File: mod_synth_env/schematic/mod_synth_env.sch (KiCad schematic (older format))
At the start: 26 parts, among them J1 AudioJack2, J2 AudioJack2, J3 Conn_02x08_Odd_Even, SW1 SW_Push, SW2 SW_SPDT, U1 TL072

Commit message: Add some footprints
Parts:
- D4: footprint (none) -> LED_THT:LED_D5.0mm
- J1, J2: footprint (none) -> Connector_Audio:Jack_3.5mm_QingPu_WQP-PJ398SM_Vertical_CircularHoles
- J3: footprint (none) -> Connector_IDC:IDC-Header_2x08_P2.54mm_Vertical
- RV1, RV2: footprint (none) -> Potentiometer_THT:Potentiometer_Alpha_RD901F-40-00D_Single_Vertical_CircularHoles
- U1: footprint (none) -> Package_DIP:DIP-8_W7.62mm_Socket_LongPads
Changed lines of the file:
@@
 EESchema Schematic File Version 4
+LIBS:mod_synth_env-cache
 EELAYER 29 0
 EELAYER END
@@
 F 0 "J3" H 3450 5742 50  0000 C CNN
 F 1 "Conn_02x08_Odd_Even" H 3450 5651 50  0000 C CNN
-F 2 "" H 3400 5225 50  0001 C CNN
+F 2 "Connector_IDC:IDC-Header_2x08_P2.54mm_Vertical" H 3400 5225 50  0001 C CNN
 F 3 "~" H 3400 5225 50  0001 C CNN
 	1    3400 5225
@@
 F 0 "J1" H 1607 3190 50  0000 C CNN
 F 1 "AudioJack2" H 1607 3099 50  0000 C CNN
-F 2 "" H 1575 2775 50  0001 C CNN
+F 2 "Connector_Audio:Jack_3.5mm_QingPu_WQP-PJ398SM_Vertical_CircularHoles" H 1575 2775 50  0001 C CNN
 F 3 "~" H 1575 2775 50  0001 C CNN
 F 4 "Gate In" H 1607 3008 50  0000 C CNN "Text"
@@
 F 0 "J2" H 1832 6915 50  0000 C CNN
 F 1 "AudioJack2" H 1832 6824 50  0000 C CNN
-F 2 "" H 1800 6500 50  0001 C CNN
+F 2 "Connector_Audio:Jack_3.5mm_QingPu_WQP-PJ398SM_Vertical_CircularHoles" H 1800 6500 50  0001 C CNN
 F 3 "~" H 1800 6500 50  0001 C CNN
 F 4 "Envelope Out" H 1832 6733 50  0000 C CNN "Text"
@@
 F 0 "RV2" H 6856 2616 50  0000 R CNN
 F 1 "1M" H 6856 2525 50  0000 R CNN
-F 2 "" H 6925 2525 50  0001 C CNN
+F 2 "Potentiometer_THT:Potentiometer_Alpha_RD901F-40-00D_Single_Vertical_CircularHoles" H 6925 2525 50  0001 C CNN
 F 3 "~" H 6925 2525 50  0001 C CNN
 F 4 "Attack" H 6856 2434 50  0000 R CNN "Text"
@@
 F 0 "RV1" H 6830 3341 50  0000 R CNN
 F 1 "1M" H 6830 3250 50  0000 R CNN
-F 2 "" H 6900 3250 50  0001 C CNN
+F 2 "Potentiometer_THT:Potentiometer_Alpha_RD901F-40-00D_Single_Vertical_CircularHoles" H 6900 3250 50  0001 C CNN
 F 3 "~" H 6900 3250 50  0001 C CNN
 F 4 "Release" H 6830 3159 50  0000 R CNN "Text"
@@
 F 0 "D4" H 3568 6245 50  0000 C CNN
 F 1 "LED" H 3568 6336 50  0000 C CNN
-F 2 "" H 3575 6500 50  0001 C CNN
+F 2 "LED_THT:LED_D5.0mm" H 3575 6500 50  0001 C CNN
 F 3 "~" H 3575 6500 50  0001 C CNN
 	1    3575 6500
@@
 F 0 "U1" H 1700 4492 50  0000 C CNN
 F 1 "TL072" H 1700 4401 50  0000 C CNN
-F 2 "" H 1700 4125 50  0001 C CNN
+F 2 "Package_DIP:DIP-8_W7.62mm_Socket_LongPads" H 1700 4125 50  0001 C CNN
 F 3 "http://www.ti.com/lit/ds/symlink/tl071.pdf" H 1700 4125 50  0001 C CNN
 	1    1700 4125

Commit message: Add footprints
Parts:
- C1, C2: footprint (none) -> Capacitor_THT:C_Disc_D9.0mm_W2.5mm_P5.00mm
- R1, R2, R3, R4, R5, R6, R7, R8, R9: footprint (none) -> Resistor_THT:R_Axial_DIN0207_L6.3mm_D2.5mm_P10.16mm_Horizontal
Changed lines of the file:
@@
 F 0 "R7" V 3668 3425 50  0000 C CNN
 F 1 "100k" V 3759 3425 50  0000 C CNN
-F 2 "" V 3805 3425 50  0001 C CNN
+F 2 "Resistor_THT:R_Axial_DIN0207_L6.3mm_D2.5mm_P10.16mm_Horizontal" V 3805 3425 50  0001 C CNN
 F 3 "~" H 3875 3425 50  0001 C CNN
 	1    3875 3425
@@
 F 0 "R8" V 4293 3425 50  0000 C CNN
 F 1 "47k" V 4384 3425 50  0000 C CNN
-F 2 "" V 4430 3425 50  0001 C CNN
+F 2 "Resistor_THT:R_Axial_DIN0207_L6.3mm_D2.5mm_P10.16mm_Horizontal" V 4430 3425 50  0001 C CNN
 F 3 "~" H 4500 3425 50  0001 C CNN
 	1    4500 3425
@@
 F 0 "R9" H 5520 2896 50  0000 L CNN
 F 1 "100k" H 5520 2805 50  0000 L CNN
-F 2 "" V 5380 2850 50  0001 C CNN
+F 2 "Resistor_THT:R_Axial_DIN0207_L6.3mm_D2.5mm_P10.16mm_Horizontal" V 5380 2850 50  0001 C CNN
 F 3 "~" H 5450 2850 50  0001 C CNN
 	1    5450 2850
@@
 F 0 "R1" H 995 4221 50  0000 L CNN
 F 1 "100k" H 995 4130 50  0000 L CNN
-F 2 "" V 855 4175 50  0001 C CNN
+F 2 "Resistor_THT:R_Axial_DIN0207_L6.3mm_D2.5mm_P10.16mm_Horizontal" V 855 4175 50  0001 C CNN
 F 3 "~" H 925 4175 50  0001 C CNN
 	1    925  4175
@@
 F 0 "R2" H 1095 4571 50  0000 L CNN
 F 1 "10k" H 1095 4480 50  0000 L CNN
-F 2 "" V 955 4525 50  0001 C CNN
+F 2 "Resistor_THT:R_Axial_DIN0207_L6.3mm_D2.5mm_P10.16mm_Horizontal" V 955 4525 50  0001 C CNN
 F 3 "~" H 1025 4525 50  0001 C CNN
 	1    1025 4525
@@
 F 0 "R3" H 1295 5696 50  0000 L CNN
 F 1 "47k" H 1295 5605 50  0000 L CNN
-F 2 "" V 1155 5650 50  0001 C CNN
+F 2 "Resistor_THT:R_Axial_DIN0207_L6.3mm_D2.5mm_P10.16mm_Horizontal" V 1155 5650 50  0001 C CNN
 F 3 "~" H 1225 5650 50  0001 C CNN
 	1    1225 5650
@@
 F 0 "R4" H 2245 6146 50  0000 L CNN
 F 1 "1k" H 2245 6055 50  0000 L CNN
-F 2 "" V 2105 6100 50  0001 C CNN
+F 2 "Resistor_THT:R_Axial_DIN0207_L6.3mm_D2.5mm_P10.16mm_Horizontal" V 2105 6100 50  0001 C CNN
 F 3 "~" H 2175 6100 50  0001 C CNN
 	1    2175 6100
@@
 F 0 "R5" V 2093 3575 50  0000 C CNN
 F 1 "R100k" V 2184 3575 50  0000 C CNN
-F 2 "" V 2230 3575 50  0001 C CNN
+F 2 "Resistor_THT:R_Axial_DIN0207_L6.3mm_D2.5mm_P10.16mm_Horizontal" V 2230 3575 50  0001 C CNN
 F 3 "~" H 2300 3575 50  0001 C CNN
 	1    2300 3575
@@
 F 0 "R6" V 2943 6500 50  0000 C CNN
 F 1 "1k" V 3034 6500 50  0000 C CNN
-F 2 "" V 3080 6500 50  0001 C CNN
+F 2 "Resistor_THT:R_Axial_DIN0207_L6.3mm_D2.5mm_P10.16mm_Horizontal" V 3080 6500 50  0001 C CNN
 F 3 "~" H 3150 6500 50  0001 C CNN
 	1    3150 6500
@@
 F 0 "C2" H 4515 2896 50  0000 L CNN
 F 1 "10nF" H 4515 2805 50  0000 L CNN
-F 2 "" H 4438 2700 50  0001 C CNN
+F 2 "Capacitor_THT:C_Disc_D9.0mm_W2.5mm_P5.00mm" H 4438 2700 50  0001 C CNN
 F 3 "~" H 4400 2850 50  0001 C CNN
 	1    4400 2850
@@
 F 0 "C1" H 2440 4696 50  0000 L CNN
 F 1 "1uF" H 2440 4605 50  0000 L CNN
-F 2 "" H 2363 4500 50  0001 C CNN
+F 2 "Capacitor_THT:C_Disc_D9.0mm_W2.5mm_P5.00mm" H 2363 4500 50  0001 C CNN
 F 3 "~" H 2325 4650 50  0001 C CNN
 	1    2325 4650

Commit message: Start work on envelope PCB
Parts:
- SW1: footprint (none) -> Connector_PinHeader_1.00mm:PinHeader_1x02_P1.00mm_Vertical
- SW2: footprint (none) -> Connector_PinHeader_1.00mm:PinHeader_1x03_P1.00mm_Vertical
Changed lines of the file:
@@
 F 0 "SW2" H 2975 3410 50  0000 C CNN
 F 1 "SW_SPDT" H 2975 3319 50  0000 C CNN
-F 2 "" H 2975 3125 50  0001 C CNN
+F 2 "Connector_PinHeader_1.00mm:PinHeader_1x03_P1.00mm_Vertical" H 2975 3125 50  0001 C CNN
 F 3 "~" H 2975 3125 50  0001 C CNN
 	1    2975 3125
-	1    0    0    -1
-$EndComp
-$Comp
-L Switch:SW_Push SW1
-U 1 1 5D201272
-P 2375 2500
-F 0 "SW1" H 2375 2785 50  0000 C CNN
-F 1 "SW_Push" H 2375 2694 50  0000 C CNN
-F 2 "" H 2375 2700 50  0001 C CNN
-F 3 "~" H 2375 2700 50  0001 C CNN
-	1    2375 2500
 	1    0    0    -1
 $EndComp
@@
 	1950 3125 2175 3125
 Wire Wire Line
-	2475 3125 2575 3125
-Wire Wire Line
-	2575 2500 2575 3125
-Connection ~ 2575 3125
-Wire Wire Line
-	2575 3125 2775 3125
+	3900 4725 4200 4725
+Wire Wire Line
+	4200 4725 4200 4875
+Connection ~ 3900 4725
+Wire Wire Line
+	3900 4725 3900 4925
+Wire Wire Line
+	4200 5500 4200 5625
+Wire Wire Line
+	4200 5625 3900 5625
+Connection ~ 3900 5625
+Wire Wire Line
+	3900 5625 3900 5325
+Wire Wire Line
+	2000 6400 2000 5350
+Wire Wire Line
+	2000 5125 2325 5125
+Connection ~ 2650 5125
+Wire Wire Line
+	2000 6500 2175 6500
+Wire Wire Line
+	2175 6500 3000 6500
+Connection ~ 2175 6500
+Wire Wire Line
+	3300 6500 3425 6500
+$Comp
+L power:GND #PWR0105
+U 1 1 5D257A03
+P 4125 6500
+F 0 "#PWR0105" H 4125 6250 50  0001 C CNN
+F 1 "GND" H 4130 6327 50  0000 C CNN
+F 2 "" H 4125 6500 50  0001 C CNN
+F 3 "" H 4125 6500 50  0001 C CNN
+	1    4125 6500
+	1    0    0    -1
+$EndComp
+Wire Wire Line
+	3725 6500 4125 6500
+$Comp
+L power:GND #PWR0106
+U 1 1 5D25CE17
+P 5550 3425
+F 0 "#PWR0106" H 5550 3175 50  0001 C CNN
+F 1 "GND" H 5555 3252 50  0000 C CNN
+F 2 "" H 5550 3425 50  0001 C CNN
+F 3 "" H 5550 3425 50  0001 C CNN
+	1    5550 3425
+	1    0    0    -1
+$EndComp
+Wire Wire Line
+	3300 3425 3725 3425
+Connection ~ 3300 3425
+Wire Wire Line
+	3300 3425 3300 3225
+Wire Wire Line
+	4025 3425 4200 3425
+Wire Wire Line
+	4650 3425 5000 3425
+Wire Wire Line
+	5300 3425 5450 3425
+Wire Wire Line
+	1325 4675 1325 4450
+Wire Wire Line
+	1325 4450 2325 4450
+Wire Wire Line
+	2325 4450 2325 4500
+Connection ~ 1325 4675
+Wire Wire Line
+	1325 4675 1400 4675
+Wire Wire Line
+	2325 4800 2325 5125
+Connection ~ 2325 5125
+Wire Wire Line
+	2325 5125 2650 5125
+Wire Wire Line
+	4400 3000 4200 3000
+Wire Wire Line
+	4200 3000 4200 3425
+Connection ~ 4200 3425
+Wire Wire Line
+	4200 3425 4350 3425
+Wire Wire Line
+	4400 2700 3175 2700
+Wire Wire Line
+	3175 2700 3175 3025
+Wire Wire Line
+	4400 2700 5450 2700
+Connection ~ 4400 2700
+Wire Wire Line
+	5450 3000 5450 3425
+Connection ~ 5450 3425
+Wire Wire Line
+	5450 3425 5550 3425
+Wire Wire Line
+	1275 4025 925  4025
+Connection ~ 1275 4025
+Wire Wire Line
+	925  4325 925  5350
+Wire Wire Line
+	925  5350 1025 5350
+Connection ~ 2000 5350
+Wire Wire Line
+	2000 5350 2000 5125
+Wire Wire Line
+	1400 4225 1200 4225
+Wire Wire Line
+	1025 4225 1025 4375
+Wire Wire Line
+	1025 4675 1025 5350
+Connection ~ 1025 5350
+Wire Wire Line
+	1025 5350 2000 5350
+Wire Wire Line
+	1200 4225 1200 5500
+Wire Wire Line
+	1200 5500 1225 5500
+Connection ~ 1200 4225
+Wire Wire Line
+	1200 4225 1025 4225
+Wire Wire Line
+	1225 5800 1225 6750
+Wire Wire Line
+	1225 6750 2875 6750
+Wire Wire Line
+	2875 6750 2875 6000
+Connection ~ 2875 6000
+Wire Wire Line
+	2875 6000 3450 6000
+$Comp
+L power:GND #PWR0107
+U 1 1 5D29D27B
+P 2100 2675
+F 0 "#PWR0107" H 2100 2425 50  0001 C CNN
+F 1 "GND" H 2105 2502 50  0000 C CNN
+F 2 "" H 2100 2675 50  0001 C CNN
+F 3 "" H 2100 2675 50  0001 C CNN
+	1    2100 2675
+	1    0    0    -1
+$EndComp
+Wire Wire Line
+	1775 2675 2100 2675
+Wire Wire Line
+	1975 2500 2175 2500
+Wire Wire Line
+	1975 2300 1975 2500
 $Comp
 L power:+12V #PWR0104
@@
 $EndComp
 Wire Wire Line
-	1975 2300 1975 2500
-Wire Wire Line
-	1975 2500 2175 2500
-Wire Wire Line
-	3900 4725 4200 4725
-Wire Wire Line
-	4200 4725 4200 4875
-Connection ~ 3900 4725
-Wire Wire Line
-	3900 4725 3900 4925
-Wire Wire Line
-	4200 5500 4200 5625
-Wire Wire Line
-	4200 5625 3900 5625
-Connection ~ 3900 5625
-Wire Wire Line
-	3900 5625 3900 5325
-Wire Wire Line
-	2000 6400 2000 5350
-Wire Wire Line
-	2000 5125 2325 5125
-Connection ~ 2650 5125
-Wire Wire Line
-	2000 6500 2175 6500
-Wire Wire Line
-	2175 6500 3000 6500
-Connection ~ 2175 6500
-Wire Wire Line
-	3300 6500 3425 6500
-$Comp
-L power:GND #PWR0105
-U 1 1 5D257A03
-P 4125 6500
-F 0 "#PWR0105" H 4125 6250 50  0001 C CNN
-F 1 "GND" H 4130 6327 50  0000 C CNN
-F 2 "" H 4125 6500 50  0001 C CNN
-F 3 "" H 4125 6500 50  0001 C CNN
-	1    4125 6500
-	1    0    0    -1
-$EndComp
-Wire Wire Line
-	3725 6500 4125 6500
-$Comp
-L power:GND #PWR0106
-U 1 1 5D25CE17
-P 5550 3425
-F 0 "#PWR0106" H 5550 3175 50  0001 C CNN
-F 1 "GND" H 5555 3252 50  0000 C CNN
-F 2 "" H 5550 3425 50  0001 C CNN
-F 3 "" H 5550 3425 50  0001 C CNN
-	1    5550 3425
-	1    0    0    -1
-$EndComp
-Wire Wire Line
-	3300 3425 3725 3425
-Connection ~ 3300 3425
-Wire Wire Line
-	3300 3425 3300 3225
-Wire Wire Line
-	4025 3425 4200 3425
-Wire Wire Line
-	4650 3425 5000 3425
-Wire Wire Line
-	5300 3425 5450 3425
-Wire Wire Line
-	1325 4675 1325 4450
-Wire Wire Line
-	1325 4450 2325 4450
-Wire Wire Line
-	2325 4450 2325 4500
-Connection ~ 1325 4675
-Wire Wire Line
-	1325 4675 1400 4675
-Wire Wire Line
-	2325 4800 2325 5125
-Connection ~ 2325 5125
-Wire Wire Line
-	2325 5125 2650 5125
-Wire Wire Line
-	4400 3000 4200 3000
-Wire Wire Line
-	4200 3000 4200 3425
-Connection ~ 4200 3425
-Wire Wire Line
-	4200 3425 4350 3425
-Wire Wire Line
-	4400 2700 3175 2700
-Wire Wire Line
-	3175 2700 3175 3025
-Wire Wire Line
-	4400 2700 5450 2700
-Connection ~ 4400 2700
-Wire Wire Line
-	5450 3000 5450 3425
-Connection ~ 5450 3425
-Wire Wire Line
-	5450 3425 5550 3425
-Wire Wire Line
-	1275 4025 925  4025
-Connection ~ 1275 4025
-Wire Wire Line
-	925  4325 925  5350
-Wire Wire Line
-	925  5350 1025 5350
-Connection ~ 2000 5350
-Wire Wire Line
-	2000 5350 2000 5125
-Wire Wire Line
-	1400 4225 1200 4225
-Wire Wire Line
-	1025 4225 1025 4375
-Wire Wire Line
-	1025 4675 1025 5350
-Connection ~ 1025 5350
-Wire Wire Line
-	1025 5350 2000 5350
-Wire Wire Line
-	1200 4225 1200 5500
-Wire Wire Line
-	1200 5500 1225 5500
-Connection ~ 1200 4225
-Wire Wire Line
-	1200 4225 1025 4225
-Wire Wire Line
-	1225 5800 1225 6750
-Wire Wire Line
-	1225 6750 2875 6750
-Wire Wire Line
-	2875 6750 2875 6000
-Connection ~ 2875 6000
-Wire Wire Line
-	2875 6000 3450 6000
-$Comp
-L power:GND #PWR0107
-U 1 1 5D29D27B
-P 2100 2675
-F 0 "#PWR0107" H 2100 2425 50  0001 C CNN
-F 1 "GND" H 2105 2502 50  0000 C CNN
-F 2 "" H 2100 2675 50  0001 C CNN
-F 3 "" H 2100 2675 50  0001 C CNN
-	1    2100 2675
-	1    0    0    -1
-$EndComp
-Wire Wire Line
-	1775 2675 2100 2675
+	2575 3125 2775 3125
+Wire Wire Line
+	2475 3125 2575 3125
+Connection ~ 2575 3125
+Wire Wire Line
+	2575 2500 2575 3125
+$Comp
+L Switch:SW_Push SW1
+U 1 1 5D201272
+P 2375 2500
+F 0 "SW1" H 2375 2785 50  0000 C CNN
+F 1 "SW_Push" H 2375 2694 50  0000 C CNN
+F 2 "Connector_PinHeader_1.00mm:PinHeader_1x02_P1.00mm_Vertical" H 2375 2700 50  0001 C CNN
+F 3 "~" H 2375 2700 50  0001 C CNN
+	1    2375 2500
+	1    0    0    -1
+$EndComp
 $EndSCHEMATC

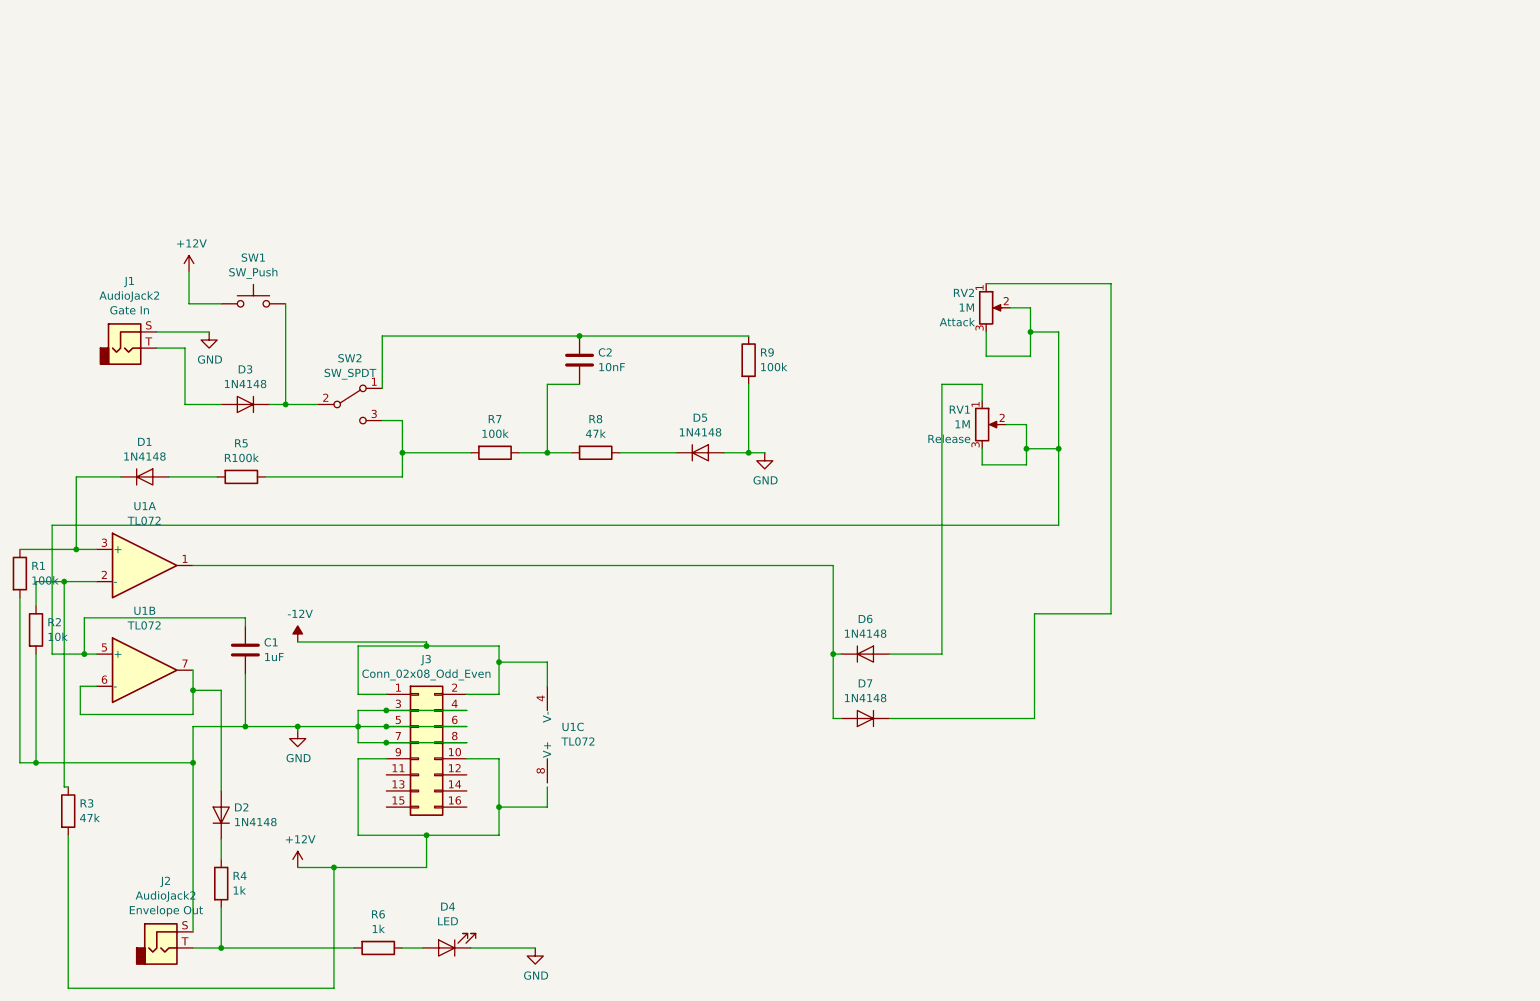
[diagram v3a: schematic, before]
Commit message: Add dual pcb for envelope
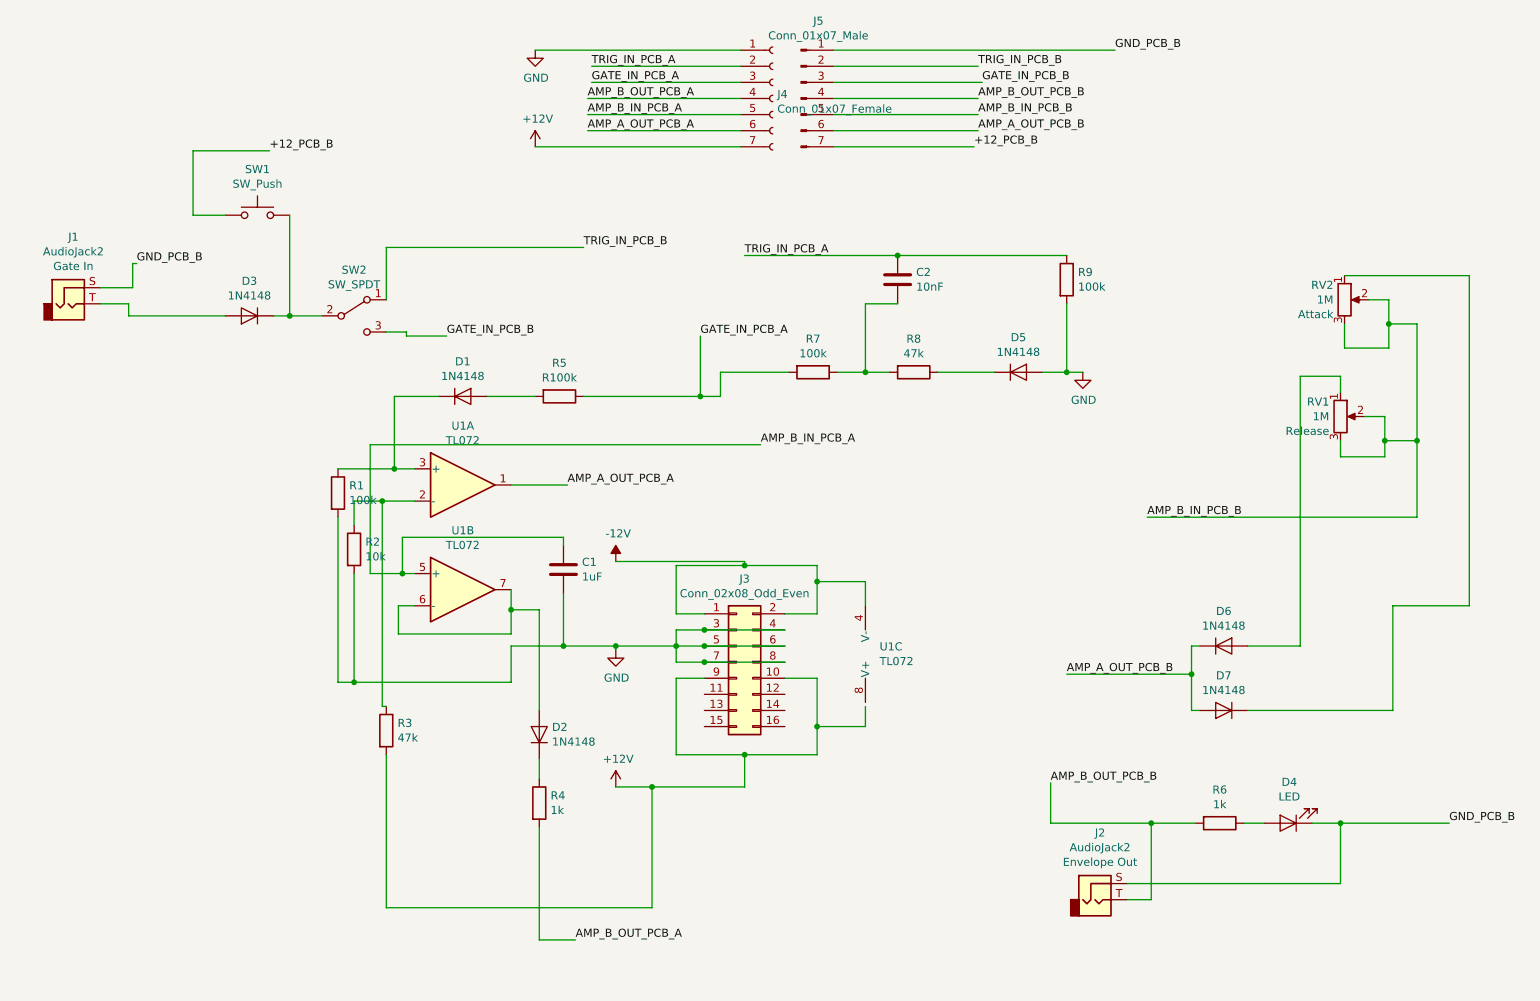
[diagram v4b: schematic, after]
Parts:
- added J4: Conn_01x07_Female, Connector_PinSocket_2.54mm:PinSocket_1x07_P2.54mm_Vertical, symbol Connector:Conn_01x07_Female
- added J5: Conn_01x07_Male, Connector_PinHeader_2.54mm:PinHeader_1x07_P2.54mm_Vertical, symbol Connector:Conn_01x07_Male
- SW1: footprint Connector_PinHeader_1.00mm:PinHeader_1x02_P1.00mm_Vertical -> Connector_PinHeader_2.54mm:PinHeader_1x02_P2.54mm_Vertical
- SW2: footprint Connector_PinHeader_1.00mm:PinHeader_1x03_P1.00mm_Vertical -> Connector_PinHeader_2.54mm:PinHeader_1x03_P2.54mm_Vertical
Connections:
- net +12V: now also J4.7 (Pin_7); no longer SW1.1
- net GND: now also J4.1 (Pin_1); no longer D4.1 (K), J1.S, J2.S
- net AMP_B_OUT_PCB_B: now reaches J2.T, R6.2
- net AMP_B_OUT_PCB_B: now also J5.4 (Pin_4); no longer R4.2
- net TRIG_IN_PCB_A: now reaches C2.1, R9.1
- net TRIG_IN_PCB_A: now also J4.2 (Pin_2); no longer SW2.1 (A)
- net GATE_IN_PCB_A: now reaches R5.1, R7.2
- net GATE_IN_PCB_A: now also J4.3 (Pin_3); no longer SW2.3 (C)
- net AMP_B_IN_PCB_B: now reaches RV1.2, RV1.3, RV2.2, RV2.3
- net AMP_B_IN_PCB_B: now also J5.5 (Pin_5); no longer C1.1, U1.5 (+)
- net AMP_A_OUT_PCB_B: now reaches D6.1 (K), D7.2 (A)
- net AMP_A_OUT_PCB_B: now also J5.6 (Pin_6); no longer U1.1
- new net +12_PCB_B: J5.7 (Pin_7), SW1.1
- new net AMP_A_OUT_PCB_A: J4.6 (Pin_6), U1.1
- new net AMP_B_IN_PCB_A: C1.1, J4.5 (Pin_5), U1.5 (+)
- new net AMP_B_OUT_PCB_A: J4.4 (Pin_4), R4.2
- new net GATE_IN_PCB_B: J5.3 (Pin_3), SW2.3 (C)
- new net GND_PCB_B: D4.1 (K), J1.S, J2.S, J5.1 (Pin_1)
- new net TRIG_IN_PCB_B: J5.2 (Pin_2), SW2.1 (A)
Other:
- moved on the sheet: C1, C2, D1, D2, D3, D4, D5, D6, D7, J1, J2, J3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

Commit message: Add footprint for SPDT mini toggle switch
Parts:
- SW2: footprint Connector_PinHeader_2.54mm:PinHeader_1x03_P2.54mm_Vertical -> mod_synth:Toggle-SPDT
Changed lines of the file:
@@
 F 0 "SW2" H 3000 2860 50  0000 C CNN
 F 1 "SW_SPDT" H 3000 2769 50  0000 C CNN
-F 2 "Connector_PinHeader_2.54mm:PinHeader_1x03_P2.54mm_Vertical" H 3000 2575 50  0001 C CNN
+F 2 "mod_synth:Toggle-SPDT" H 3000 2575 50  0001 C CNN
 F 3 "~" H 3000 2575 50  0001 C CNN
 	1    3000 2575

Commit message: Update footprint for env
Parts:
- SW2: footprint mod_synth:Toggle-SPDT -> mod_synth:SPDT_Switch_Vertical
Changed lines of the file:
@@
 F 0 "SW2" H 3000 2860 50  0000 C CNN
 F 1 "SW_SPDT" H 3000 2769 50  0000 C CNN
-F 2 "mod_synth:Toggle-SPDT" H 3000 2575 50  0001 C CNN
+F 2 "mod_synth:SPDT_Switch_Vertical" H 3000 2575 50  0001 C CNN
 F 3 "~" H 3000 2575 50  0001 C CNN
 	1    3000 2575

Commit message: Move PCB labels
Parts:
- R5: value R100k -> 100k or 10k
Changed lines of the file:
@@
 P 4275 3075
 F 0 "R5" V 4068 3075 50  0000 C CNN
-F 1 "R100k" V 4159 3075 50  0000 C CNN
+F 1 "100k or 10k" V 4159 3075 50  0000 C CNN
 F 2 "Resistor_THT:R_Axial_DIN0207_L6.3mm_D2.5mm_P10.16mm_Horizontal" V 4205 3075 50  0001 C CNN
 F 3 "~" H 4275 3075 50  0001 C CNN

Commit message: Add missing +12v to U1
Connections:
- net +12V: now also U1.8 (V+)
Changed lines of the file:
@@
 	5875 4225 5875 4425
-Wire Wire Line
-	6175 5000 6175 5125
 Wire Wire Line
 	6175 5125 5875 5125
@@
 Wire Wire Line
 	5975 1525 6850 1525
+Wire Wire Line
+	6175 4975 6175 5125
 $EndSCHEMATC
